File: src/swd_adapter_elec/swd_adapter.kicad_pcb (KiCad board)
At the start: 2 copper layers, 10.2 x 9.5 mm, 2 parts, among them J101 Conn_01x06_Pin, J102 Conn_01x14_Pin

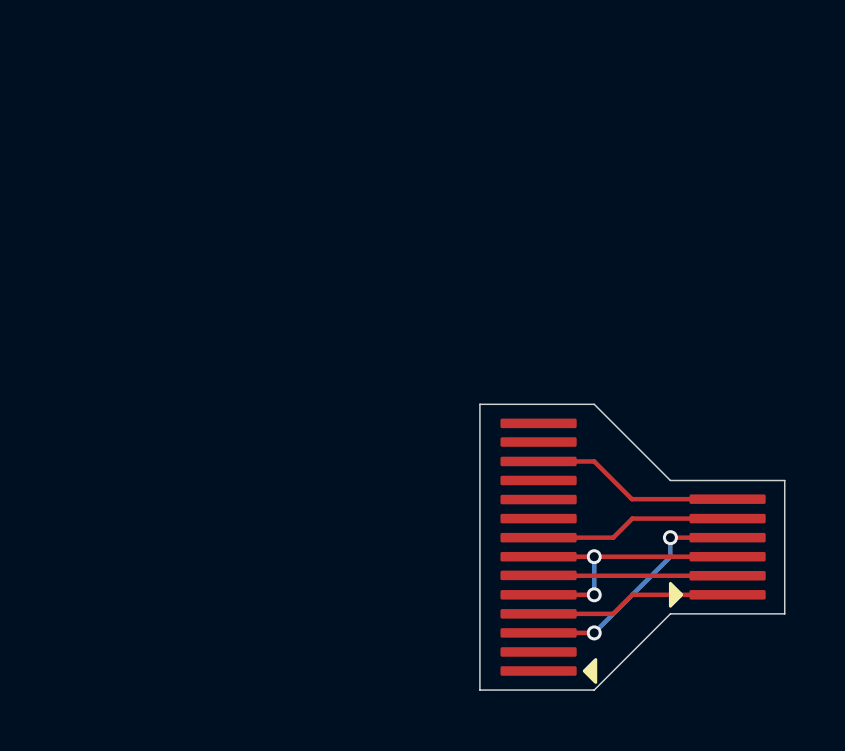
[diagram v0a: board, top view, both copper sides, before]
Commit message: The IDC 14 pin to 6 pin converter
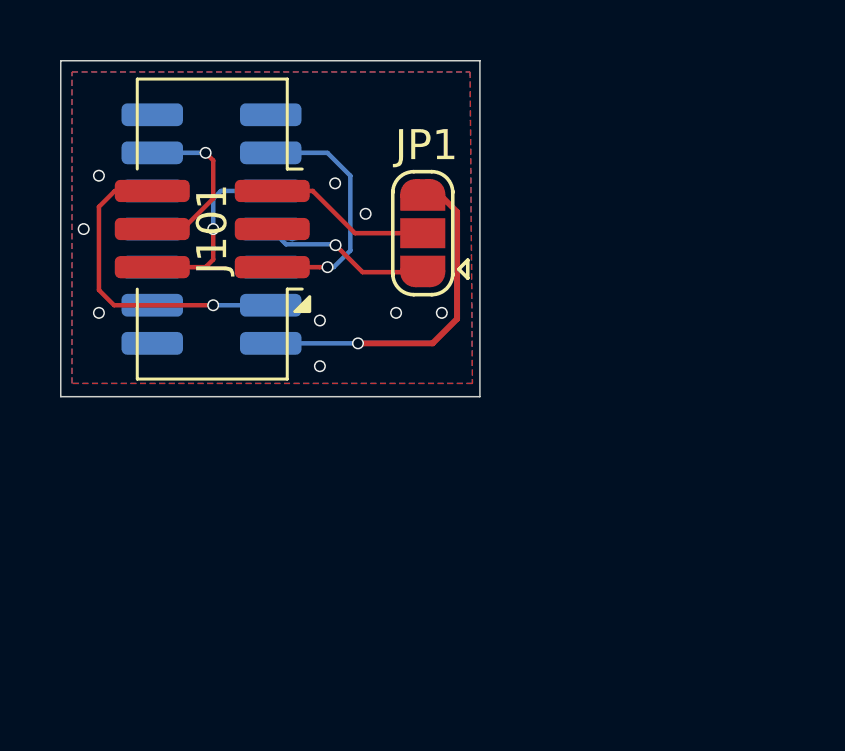
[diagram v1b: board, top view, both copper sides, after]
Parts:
- added JP1: SolderJumper_3_Open, Jumper:SolderJumper-3_P1.3mm_Open_RoundedPad1.0x1.5mm, F.Cu at (-1.91, -5.71)
- J101: footprint Bluesat:IDC6-pad -> Bluesat:IDC6
- J102: footprint Bluesat:IDC14-pad -> Bluesat:IDC14-Plug-Flipped; moved to B.Cu
- moved J101 19.4 mm to (-8.92, -5.84), turned to 90 degrees
- moved J102 12.7 mm to (-8.95, -5.84), turned to 90 degrees
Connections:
- J101 pad 5: /SWO -> /SWO/UARTRX
- J102 pad 14: unconnected-(J102-Pin_14-Pad14) -> /UARTRX
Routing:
- net /UARTRX: track 0.00 -> 11.5 mm, vias 0 -> 1
- net /GND: track 8.89 -> 0.95 mm, vias 2 -> 9
- net /SWO/UARTRX: track 0.00 -> 5.60 mm
- net /NRST: track 6.24 -> 10.7 mm, vias 0 -> 1
- net /SWDIO: track 5.98 -> 8.42 mm, vias 0 -> 1
- net /SWCLK: track 5.71 -> 7.44 mm, vias 0 -> 1
- net /VDD: track 7.40 -> 7.11 mm, vias 2 -> 1
- net /SWO: track 5.98 -> 5.85 mm, vias 0 -> 1
- added copper zone on B.Cu, net /GND
- added copper zone on F.Cu, net /GND
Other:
- board size 10.2 x 9.5 mm -> 14 x 11.2 mm

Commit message: Final touches
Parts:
- added G***: LOGO, Project:Reindeer, B.Cu at (-2.50, -3.75)
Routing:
- net /SWCLK: track 7.44 -> 6.91 mm
- net /GND: vias 9 -> 10
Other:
- outline, holes or cut-outs redrawn

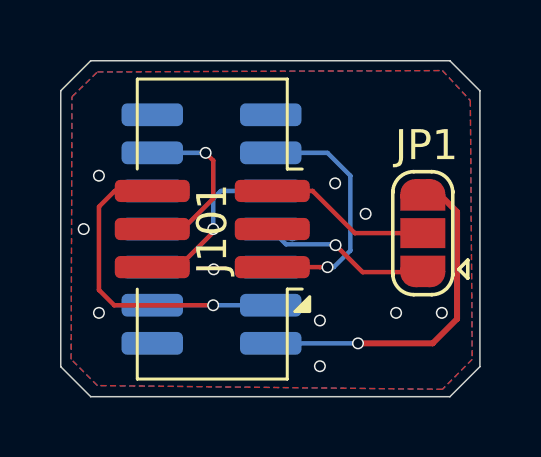
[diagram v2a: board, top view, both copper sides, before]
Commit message: Fix IDC6 pinout :sob:, reroute
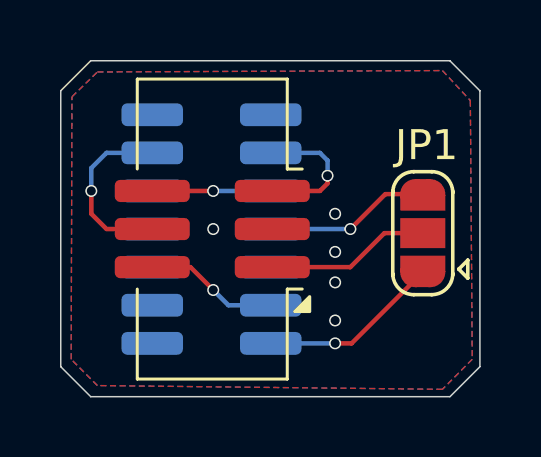
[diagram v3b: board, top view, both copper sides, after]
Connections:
- net /VDD renamed /T_VCC
- J101 pad 1: /SWDIO -> /SWO/UART
- J101 pad 2: /SWCLK -> /NRST
- J101 pad 5: /SWO/UARTRX -> /SWDIO
- J101 pad 6: /NRST -> /SWCLK
- J102 pad 14: /UARTRX -> /T_VCP_TX
- JP1 pad 1: /SWO -> /T_VCP_TX
- JP1 pad 2: /SWO/UARTRX -> /SWO/UART
- JP1 pad 3: /UARTRX -> /SWO
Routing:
- net /UARTRX: track 11.5 -> 0.00 mm, vias 1 -> 0
- net /T_VCP_TX: track 0.00 -> 6.05 mm, vias 0 -> 1
- net /SWO/UARTRX: track 5.60 -> 0.00 mm
- net /SWO/UART: track 0.00 -> 5.49 mm
- net /NRST: track 10.7 -> 5.73 mm
- net /SWDIO: track 8.42 -> 4.71 mm
- net /SWCLK: track 6.91 -> 3.95 mm
- net /T_VCC: track 7.11 -> 8.27 mm
- net /GND: vias 10 -> 5

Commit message: [ELEC] REV markers on all PCB's, Fix USB hub passives
Add mounting holes to all PCB schematics
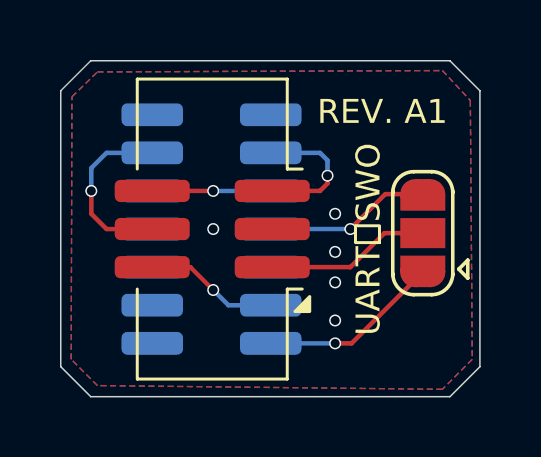
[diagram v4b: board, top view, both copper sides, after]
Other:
- board text added: "REV. A1"
- board text added: "UARTーSWO"
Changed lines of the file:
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@@
 		(tenting front back)
 		(pcbplotparams
-			(layerselection 0x00000000_00000000_55555555_5755f5ff)
+			(layerselection 0x00000000_00000000_55555555_5555f550)
 			(plot_on_all_layers_selection 0x00000000_00000000_00000000_00000000)
 			(disableapertmacros no)
@@
 			(crossoutdnponfab yes)
 			(subtractmaskfromsilk no)
-			(outputformat 1)
+			(outputformat 5)
 			(mirror no)
 			(drillshape 0)
@@
 			(at 2.931 0.127 180)
 			(layer "F.SilkS")
+			(hide yes)
 			(effects
 				(font
@@
 		(layer "Edge.Cuts")
 	)
+	(gr_text "UARTーSWO"
+		(at -3.25 -5.5 90)
+		(layer "F.SilkS")
+		(effects
+			(font
+				(size 0.8 0.8)
+				(thickness 0.1)
+			)
+			(justify bottom)
+		)
+	)
+	(gr_text "REV. A1"
+		(at -3.25 -9.75 0)
+		(layer "F.SilkS")
+		(effects
+			(font
+				(size 0.8 0.8)
+				(thickness 0.1)
+			)
+		)
+	)
 	(segment
